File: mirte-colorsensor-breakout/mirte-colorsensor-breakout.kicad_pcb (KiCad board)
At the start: 2 copper layers, 27.9 x 14 mm, 3 parts, among them J1 JST xh 4 pin pcb, J2 color sensor header

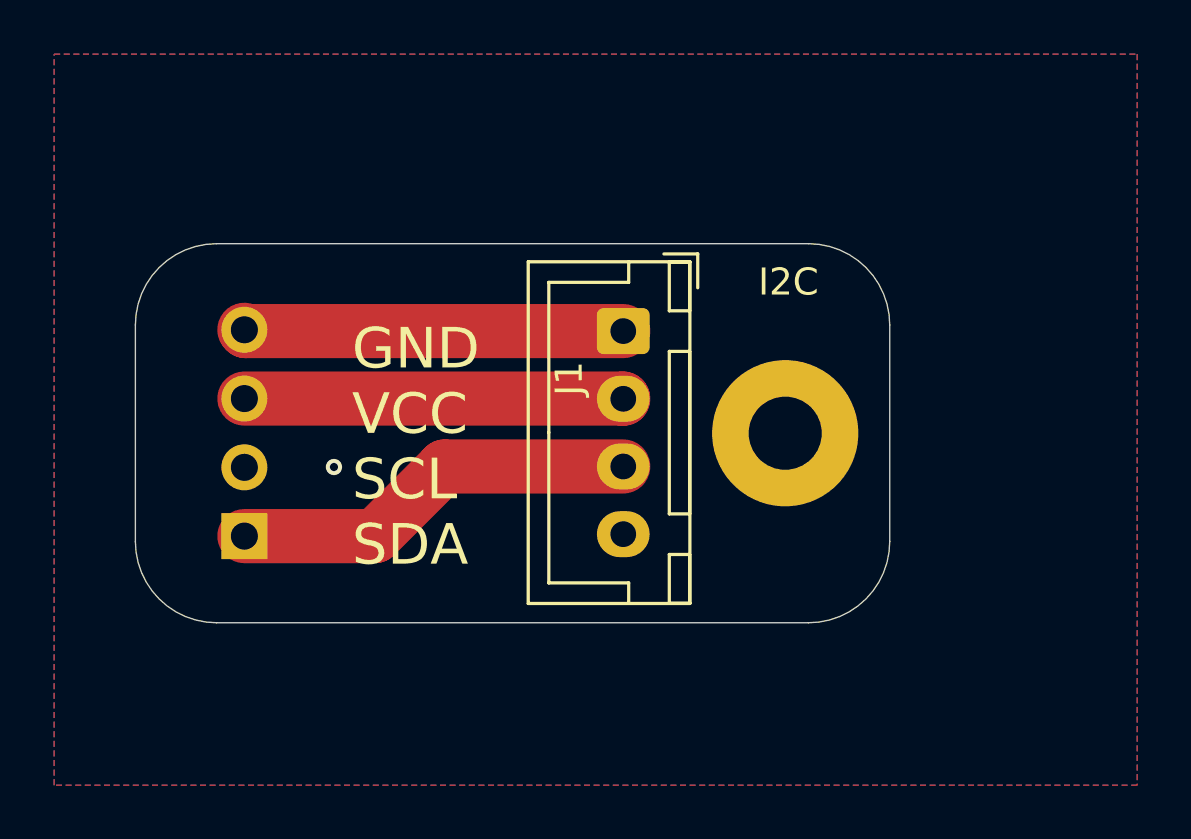
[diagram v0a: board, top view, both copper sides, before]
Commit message: mirte modules back!
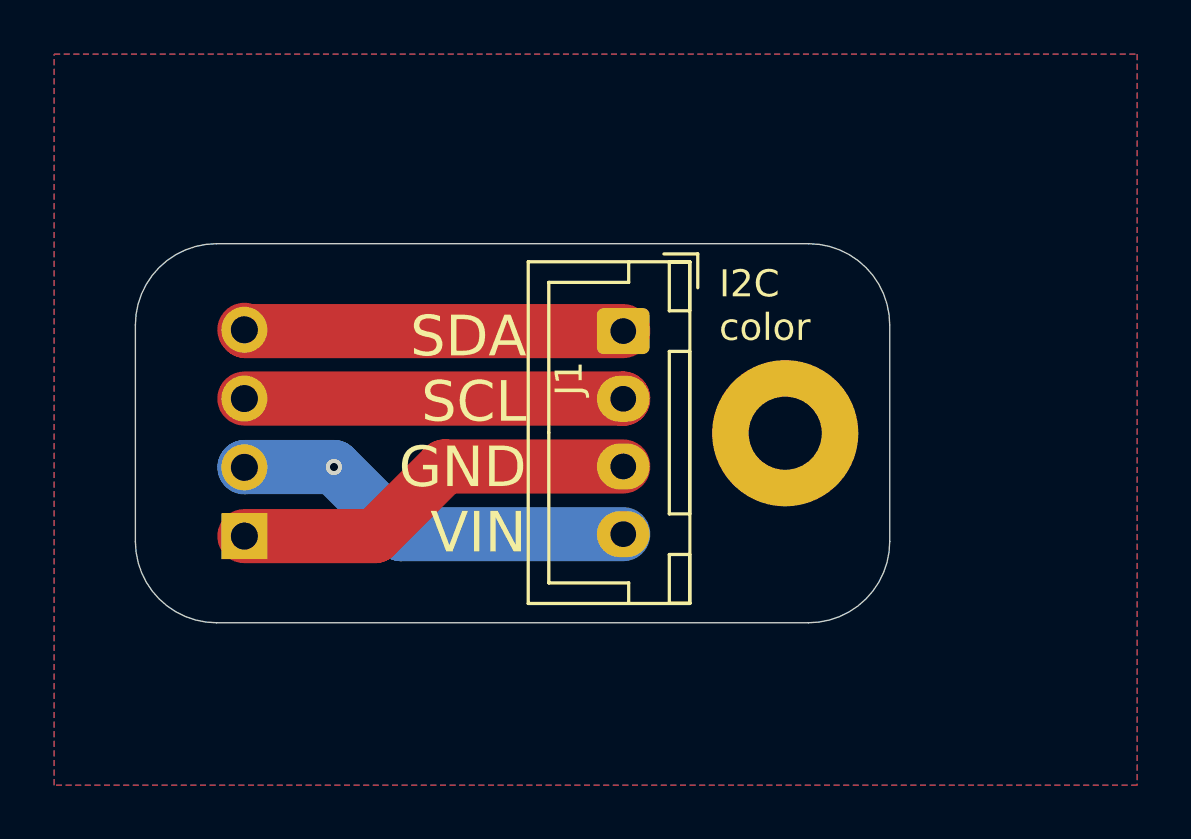
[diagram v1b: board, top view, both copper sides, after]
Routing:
- net /GND: track 0.00 -> 15.0 mm
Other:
- board text added: "I2C color"
- board text added: "SDA SCL GND VCC"
- board text added: "SDA SCL GND VIN"
- board text removed: "GND VCC SCL SDA"
- board text removed: "I2C"
- board text removed: "VCC GND SCL SDA"
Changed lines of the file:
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@@
 		)
+	)
+	(gr_rect
+		(start 127.254 72.39)
+		(end 138.43 83.566)
+		(stroke
+			(width 0.1)
+			(type default)
+		)
+		(fill none)
+		(layer "B.SilkS")
 	)
 	(gr_line
@@
 		(layer "User.1")
 	)
-	(gr_text "VCC\nGND\nSCL\nSDA"
+	(gr_text "SDA\nSCL\nGND\nVCC"
 		(at 135 82.5 0)
 		(layer "B.SilkS")
@@
 		)
 	)
-	(gr_text "GND\nVCC\nSCL\nSDA"
-		(at 133 83 0)
+	(gr_text "SDA\nSCL\nGND\nVIN"
+		(at 139.446 82.55 0)
 		(layer "F.SilkS")
 		(effects
@@
 				(thickness 0.2)
 			)
-			(justify left bottom)
-		)
-	)
-	(gr_text "I2C"
-		(at 148 73 0)
+			(justify right bottom)
+		)
+	)
+	(gr_text "I2C\ncolor"
+		(at 146.558 74.676 0)
 		(layer "F.SilkS")
 		(effects
@@
 		(net 3)
 	)
+	(segment
+		(start 132.334 79.248)
+		(end 129.037 79.248)
+		(width 2)
+		(layer "B.Cu")
+		(net 3)
+	)
+	(segment
+		(start 143.019 81.728)
+		(end 134.814 81.728)
+		(width 2)
+		(layer "B.Cu")
+		(net 3)
+	)
+	(segment
+		(start 134.814 81.728)
+		(end 132.334 79.248)
+		(width 2)
+		(layer "B.Cu")
+		(net 3)
+	)
+	(segment
+		(start 129.037 79.248)
+		(end 129.025 79.26)
+		(width 2)
+		(layer "B.Cu")
+		(net 3)
+	)
